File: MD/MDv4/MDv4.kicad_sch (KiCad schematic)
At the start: 42 parts, among them J1 XT60PW-M, J2 XT60PW-M, J3 XT30PW-M, J4 XT30PW-M

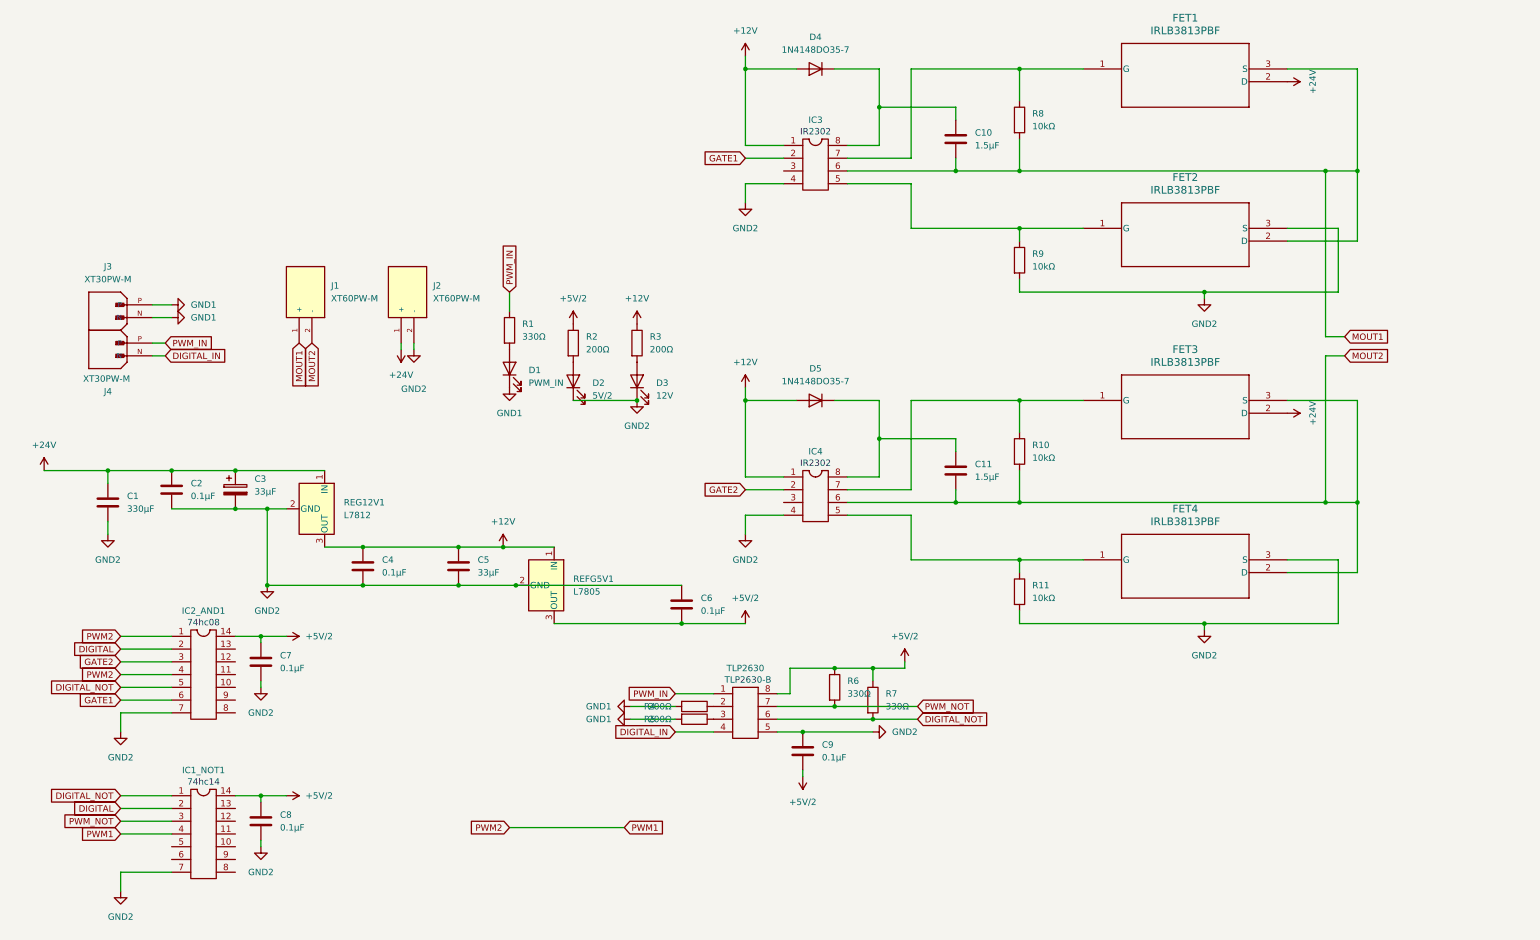
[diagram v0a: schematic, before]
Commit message: メイン基板変更進捗
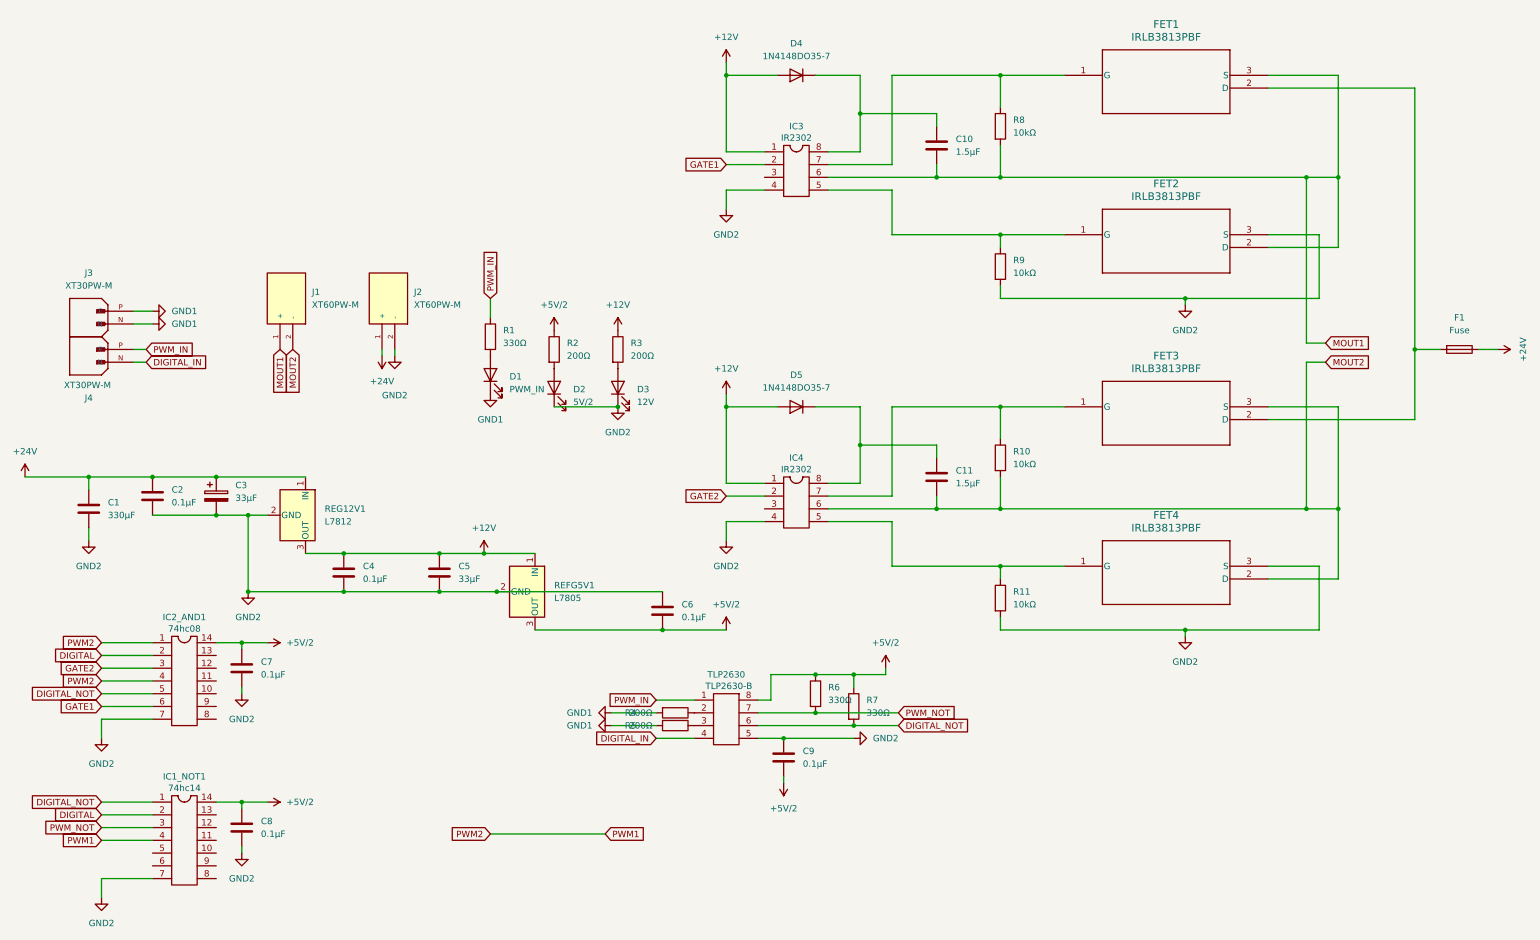
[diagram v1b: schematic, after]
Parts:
- added F1: Fuse, Library:FUSE_3557-15, symbol Device:Fuse
- C10, C11, C2, C4, C6, C7, C8, C9: footprint Capacitor_SMD:C_0603_1608Metric -> Library:C_Disc_D11.0mm_W5.0mm_P5.0mm_kai
- R1, R10, R11, R2, R3, R4, R5, R6, R7, R8, R9: footprint Resistor_SMD:R_0603_1608Metric -> Library:R_Axial_DIN0207_L6.3mm_D2.5mm_P10.16mm_Horizontal_kai
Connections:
- net +24V: now also F1.1; no longer FET1.2 (D), FET3.2 (D)
- new net: F1.2, FET1.2 (D), FET3.2 (D)
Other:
- moved on the sheet: C1, C10, C11, C2, C3, C4, C5, C6, C7, C8, C9, D1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
